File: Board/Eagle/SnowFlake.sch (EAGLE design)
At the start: 50 parts, among them IC1 ATSAMD20E-TQFP32, J2 CON-SNOWF-IN, J3 CON-SNOWF-OUT

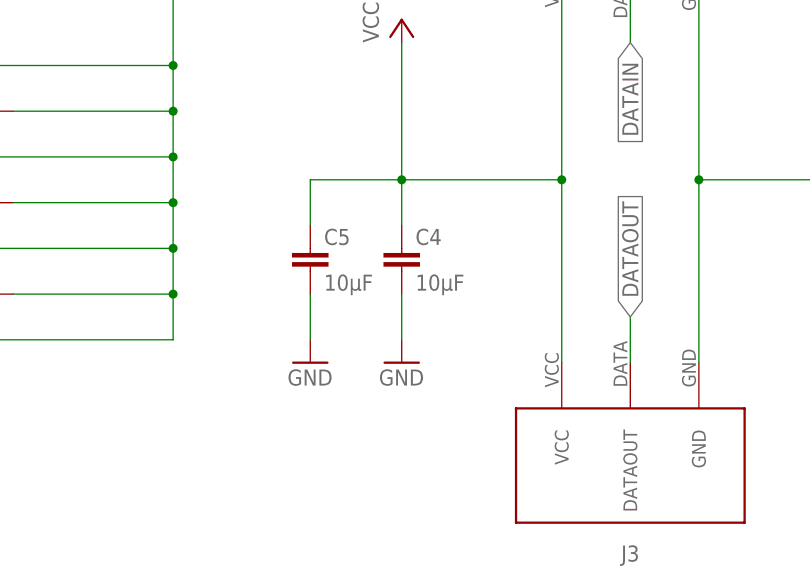
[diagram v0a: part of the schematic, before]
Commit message: Fixing the capacitor value in the schema from 10µF to 1µF.
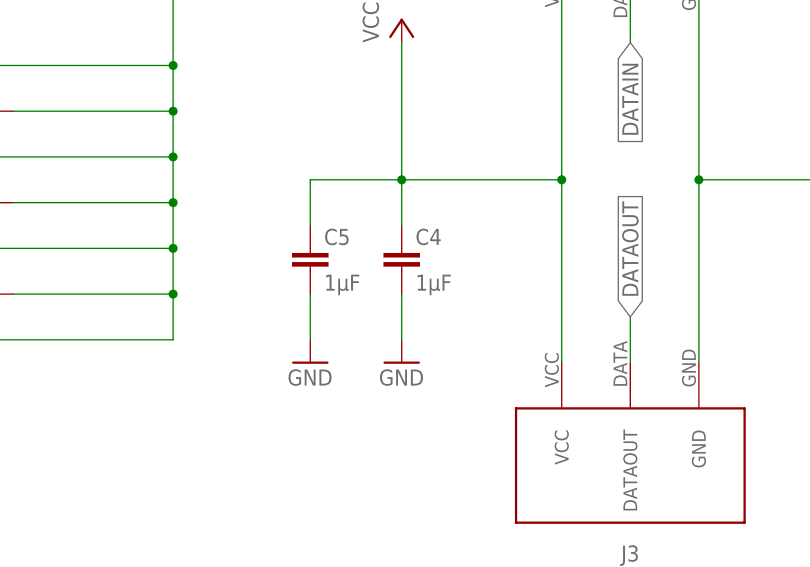
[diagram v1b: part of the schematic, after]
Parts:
- C4, C5: value 10µF -> 1µF
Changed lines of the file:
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@@
 <?xml version="1.0" encoding="utf-8"?>
 <!DOCTYPE eagle SYSTEM "eagle.dtd">
-<eagle version="8.3.2">
+<eagle version="8.5.1">
 <drawing>
 <settings>
-<setting alwaysvectorfont="no"/>
+<setting alwaysvectorfont="yes"/>
 <setting verticaltext="up"/>
 </settings>
@@
 <part name="P+8" library="supply1" library_urn="urn:adsk.eagle:library:371" deviceset="VCC" device=""/>
 <part name="GND4" library="supply1" library_urn="urn:adsk.eagle:library:371" deviceset="GND" device=""/>
-<part name="C4" library="lucky-resistor" library_urn="urn:adsk.eagle:library:481313" deviceset="C" device="0805-MURATA-GRM-21" package3d_urn="urn:adsk.eagle:package:481485/1" value="10µF"/>
+<part name="C4" library="lucky-resistor" library_urn="urn:adsk.eagle:library:481313" deviceset="C" device="0805-MURATA-GRM-21" package3d_urn="urn:adsk.eagle:package:481485/1" value="1µF"/>
 <part name="GND5" library="supply1" library_urn="urn:adsk.eagle:library:371" deviceset="GND" device=""/>
-<part name="C5" library="lucky-resistor" library_urn="urn:adsk.eagle:library:481313" deviceset="C" device="0805-MURATA-GRM-21" package3d_urn="urn:adsk.eagle:package:481485/1" value="10µF"/>
+<part name="C5" library="lucky-resistor" library_urn="urn:adsk.eagle:library:481313" deviceset="C" device="0805-MURATA-GRM-21" package3d_urn="urn:adsk.eagle:package:481485/1" value="1µF"/>
 <part name="GND6" library="supply1" library_urn="urn:adsk.eagle:library:371" deviceset="GND" device=""/>
 <part name="C6" library="lucky-resistor" library_urn="urn:adsk.eagle:library:481313" deviceset="C" device="0805-MURATA-GRM-21" package3d_urn="urn:adsk.eagle:package:481485/1" value="100nF"/>
